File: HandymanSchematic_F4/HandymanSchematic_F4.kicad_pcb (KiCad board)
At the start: 4 copper layers, 55.6 x 45.5 mm, 85 parts, among them J1 SWD Header, J2 PWR, J3 JACKS, J4 FOOTSWITCH, J5 ScopeGroundLoop, Q1 BC847, Q2 2N7002, Q3 2N7002, SW1 RST, SW2 BYP, U1 TL074, U2 TL074, U3 STM32G030F6P6, U4 AMS1117, U5 SSD1306

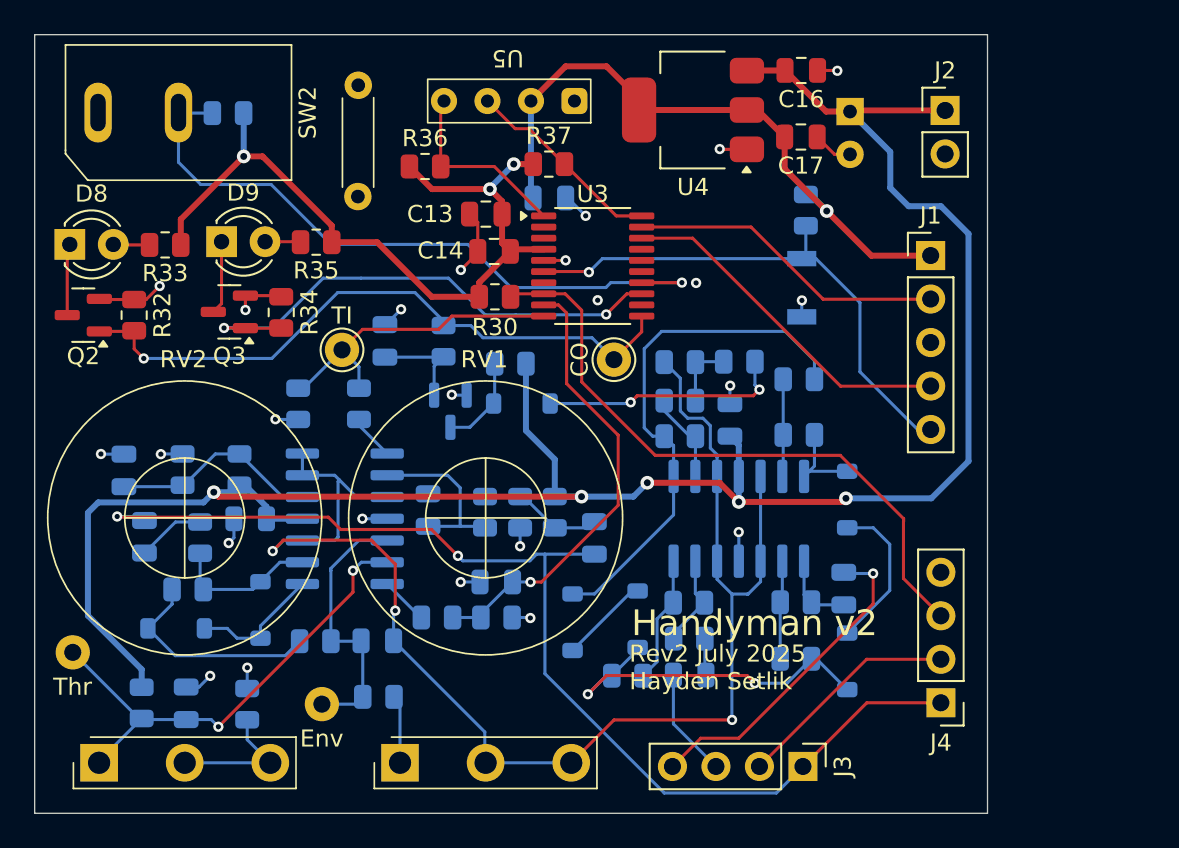
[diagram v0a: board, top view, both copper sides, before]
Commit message: switched to firmware env, new layout
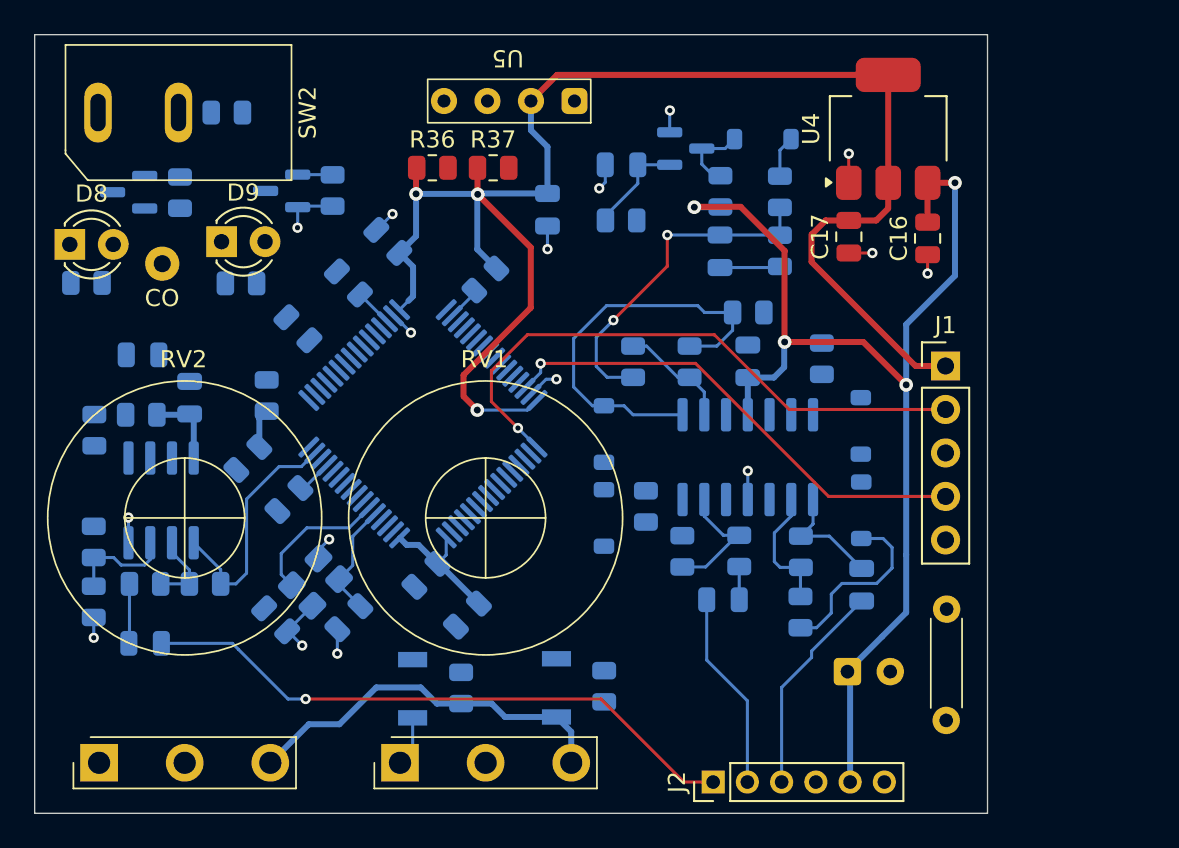
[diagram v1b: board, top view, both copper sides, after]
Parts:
- removed C8: 100n, Capacitor_SMD:C_0805_2012Metric
- removed C9: 22n, Capacitor_SMD:C_0805_2012Metric
- removed D2, D3: 1N4148W, Diode_SMD:D_SOD-123
- removed J3: JACKS, Connector_PinHeader_2.54mm:PinHeader_1x04_P2.54mm_Vertical
- removed J4: FOOTSWITCH, Connector_PinHeader_2.54mm:PinHeader_1x04_P2.54mm_Vertical
- removed R11: 1k, Resistor_SMD:R_0805_2012Metric
- removed R14: 5k6, Resistor_SMD:R_0805_2012Metric
- removed R16, R17: 56k, Resistor_SMD:R_0805_2012Metric
- removed R20: 180k, Resistor_SMD:R_0805_2012Metric
- removed R23, R4, R6: 100k, Resistor_SMD:R_0805_2012Metric
- removed TP1: Thr, TestPoint:TestPoint_THTPad_D2.0mm_Drill1.0mm_VAL
- removed TP3: Env, TestPoint:TestPoint_THTPad_D2.0mm_Drill1.0mm_VAL
- removed TP7: TI, TestPoint:TestPoint_THTPad_D2.0mm_Drill1.0mm_VAL
- removed U1: TL074, Package_SO:SOIC-14_3.9x8.7mm_P1.27mm
- added C15: 4u7, Capacitor_SMD:C_0805_2012Metric, B.Cu at (18.3, 14.5)
- added C18: 10u, Capacitor_SMD:C_0805_2012Metric, B.Cu at (12.4, 24.8)
- added C21: 6p, Capacitor_SMD:C_0805_2012Metric, B.Cu at (14.1, 34.2)
- added C22: 6p, Capacitor_SMD:C_0805_2012Metric, B.Cu at (18.4, 34.0)
- added C23: 1u, Capacitor_SMD:C_0805_2012Metric, B.Cu at (6.45, 35.5)
- added R310: 100k, Resistor_SMD:R_0805_2012Metric, B.Cu at (33.3, 38.1)
- added SW302: BOOT, Button_Switch_SMD:SW_SPST_B3U-1000P, B.Cu at (30.5, 38.1)
- added U6: TL072, Package_SO:SOIC-8_3.9x4.9mm_P1.27mm, B.Cu at (7.38, 27.2)
- added Y1: 16MHz, Crystal:Crystal_SMD_3225-4Pin_3.2x2.5mm, B.Cu at (16.4, 32.0)
- C11: value 1u -> 47n
- C12: value 10n -> 100n
- C13, C14, Q2, Q3, R30, R32, R33, R34, R35, TP8: moved to B.Cu
- C7: value 1u -> 100n
- J2: value PWR -> JACKS; footprint Connector_PinHeader_2.54mm:PinHeader_1x02_P2.54mm_Vertical -> Connector_PinHeader_2.00mm:PinHeader_1x06_P2.00mm_Vertical
- J5: footprint Connector:THT_GND_WIRE -> Connector_Wire:THT_GND_WIRE
- R24: value 470k -> 47k
- R25: value 470k -> 220k
- R26: value 47k -> 330k
- R27: value 180k -> 22
- R28: value 100k -> 47k
- U3: value STM32G030F6P6 -> STM32F411RETx; footprint Package_SO:TSSOP-20_4.4x6.5mm_P0.65mm -> Package_QFP:LQFP-64_10x10mm_P0.5mm; moved to B.Cu
- moved J5 45.8 mm to (53.2, 36.6), turned to 90 degrees
- moved J2 41.5 mm to (39.6, 43.6), turned to 90 degrees
- moved R29 34.4 mm to (24.9, 38.2), turned to 90 degrees
- moved C19 32.7 mm to (47.5, 37.2), turned to 0 degrees
- moved SW1 32.6 mm to (22.1, 38.2)
- moved R24 27.4 mm to (3.45, 33.1), turned to -90 degrees
- moved TP8 27.0 mm to (7.45, 13.4), turned to 180 degrees
- moved C13 23.4 mm to (25.3, 33.9), turned to 45 degrees
- moved C7 23.3 mm to (20.6, 12.1), turned to -45 degrees
- moved R25 22.3 mm to (6.45, 32.1), turned to 0 degrees
- moved D1 20.9 mm to (42.5, 6.10)
- moved Q1 20.6 mm to (38.0, 6.65), turned to 0 degrees
- moved C14 19.3 mm to (22.9, 31.6), turned to 45 degrees
- moved C11 18.3 mm to (40.0, 12.7), turned to -90 degrees
- moved C4 17.2 mm to (34.3, 7.60), turned to 180 degrees
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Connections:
- C11 pad 1: FX_IN -> Net-(C11-Pad1)
- C11 pad 2: Net-(C11-Pad2) -> /Analog/VG
- C12 pad 1: /Analog/VG -> GND
- C12 pad 2: Net-(U1C--) -> +3.3VA
- C5 pad 1: FX_IN -> GND
- C5 pad 2: Net-(C5-Pad2) -> +3.3V
- C7 pad 1: /Analog/Env -> GND
- C7 pad 2: /Analog/VG -> +3.3V
- J2 pad 1: +9V -> FX_IN
- J2 pad 2: GND -> LOOP_IN
- R10 pad 1: Net-(R10-Pad1) -> Net-(C11-Pad1)
- R24 pad 1: Net-(C11-Pad2) -> Net-(U6A-+)
- R24 pad 2: +9V -> GND
- R25 pad 1: GND -> Net-(C23-Pad2)
- R25 pad 2: Net-(C11-Pad2) -> Net-(U6A--)
- R26 pad 1: Net-(C11-Pad2) -> Net-(U6A--)
- R26 pad 2: Net-(U1C--) -> TUNE_IN
- R27 pad 1: Net-(R27-Pad1) -> +3.3V
- R27 pad 2: TUNE_IN -> +3.3VA
- R28 pad 1: GND -> +3.3V
- R28 pad 2: TUNE_IN -> Net-(U6A-+)
- R7 pad 2: Net-(R10-Pad1) -> Net-(C11-Pad1)
- R9 pad 1: Net-(R10-Pad1) -> Net-(C11-Pad1)
- RV1 pad 1: Net-(R14-Pad2) -> GND
- RV1 pad 2: /Analog/VG -> THRESH_IN
- RV1 pad 3: /Analog/VG -> +3.3V
- RV2 pad 1: /Analog/Thresh -> GND
- RV2 pad 2: Net-(R17-Pad1) -> RELEASE_IN
- RV2 pad 3: Net-(R17-Pad1) -> +3.3V
- U3 pad 1: /Digital/SDA -> +3.3V
- U3 pad 10: TUNE_IN -> unconnected-(U3-PC2-Pad10)
- U3 pad 11: CLOSED_OUT -> unconnected-(U3-PC3-Pad11)
- U3 pad 12: unconnected-(U3-PA5-Pad12) -> GND
- U3 pad 13: /Digital/GateLED -> +3.3VA
- U3 pad 14: /Digital/GateByp -> unconnected-(U3-PA0-Pad14)
- U3 pad 15: unconnected-(U3-PB0/PB1/PB2/PA8-Pad15) -> TUNE_IN
- U3 pad 16: unconnected-(U3-PA11/PA9-Pad16) -> THRESH_IN
- U3 pad 17: unconnected-(U3-PA12/PA10-Pad17) -> RELEASE_IN
- U3 pad 18: SWDIO -> GND
- U3 pad 19: SWCLK -> +3.3V
- U3 pad 20: /Digital/SCL -> unconnected-(U3-PA4-Pad20)
- U3 pad 4: +3.3V -> unconnected-(U3-PC15-Pad4)
- U3 pad 5: GND -> Net-(U3-PH0)
- U3 pad 6: NRST -> Net-(U3-PH1)
- U3 pad 7: unconnected-(U3-PA0-Pad7) -> NRST
- U3 pad 8: /Digital/TunerModeIn -> unconnected-(U3-PC0-Pad8)
- U3 pad 9: OPEN_IN -> unconnected-(U3-PC1-Pad9)
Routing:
- net /Analog/VG: track 85.3 -> 3.53 mm, vias 3 -> 0
- net +9V: track 123.0 -> 73.2 mm, vias 5 -> 4
- net +3.3V: track 83.5 -> 125.4 mm, vias 4 -> 3
- net /Digital/GateByp: track 39.8 -> 0.00 mm, vias 1 -> 0
- net CLOSED_OUT: track 37.9 -> 0.00 mm, vias 1 -> 0
- net /Digital/TunerModeIn: track 37.5 -> 2.00 mm
- net NRST: track 31.5 -> 0.00 mm, vias 1 -> 0
- net FX_IN: track 66.0 -> 35.6 mm, vias 2 -> 1
- net /Analog/Thresh: track 28.5 -> 0.00 mm, vias 2 -> 0
- net /Digital/GateLED: track 30.3 -> 2.04 mm, vias 2 -> 0
- net OPEN_IN: track 26.5 -> 0.00 mm, vias 1 -> 0
- net Net-(C11-Pad1): track 0.00 -> 20.0 mm, vias 0 -> 2
- net SWCLK: track 18.6 -> 34.8 mm, vias 0 -> 1
- net /Analog/Env: track 15.9 -> 0.00 mm
- net FX_OUT: track 13.2 -> 0.00 mm
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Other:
- board text removed: "CLK"
- board text removed: "DIO"
- board text removed: "FI"
- board text removed: "FO"
- board text removed: "GND"
- board text removed: "Handyman v2"
- board text removed: "LI"
- board text removed: "LO"
- board text removed: "NRST"
- board text removed: "Rev2 July 2025 Hayden Setlik"
- board text removed: "VCC"

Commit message: prelim routing
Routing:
- net +3.3V: track 125.4 -> 257.9 mm, vias 3 -> 5
- net /Analog/VG: track 3.53 -> 81.8 mm, vias 0 -> 4
- net CLOSED_OUT: track 0.00 -> 77.1 mm, vias 0 -> 1
- net NRST: track 0.00 -> 48.3 mm, vias 0 -> 3
- net +9V: track 73.2 -> 120.4 mm, vias 4 -> 5
- net THRESH_IN: track 0.00 -> 46.8 mm, vias 0 -> 2
- net /Digital/TunerModeIn: track 2.00 -> 44.9 mm, vias 0 -> 1
- net RELEASE_IN: track 0.00 -> 33.5 mm, vias 0 -> 1
- net /Digital/GateByp: track 0.00 -> 32.9 mm, vias 0 -> 2
- net /Digital/SCL: track 0.00 -> 26.7 mm, vias 0 -> 1
- net /Digital/SDA: track 0.00 -> 26.5 mm, vias 0 -> 1
- net /Digital/GateLED: track 2.04 -> 26.6 mm, vias 0 -> 2
- net GND: track 29.6 -> 52.9 mm, vias 16 -> 32
- net /Analog/SumPt: track 10.7 -> 29.5 mm
- net /Digital/BOOT0: track 0.00 -> 13.6 mm
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
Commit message: prettier routing, DRC passing
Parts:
- added TP1: AC, TestPoint:TestPoint_THTPad_D2.0mm_Drill1.0mm_VAL, F.Cu at (31.9, 15.2)
- added TP2: AA, TestPoint:TestPoint_THTPad_D2.0mm_Drill1.0mm_VAL, F.Cu at (47.9, 16.1)
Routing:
- net +9V: track 120.4 -> 129.2 mm
- net /Analog/VG: track 81.8 -> 89.5 mm, vias 4 -> 2
- net +3.3V: track 257.9 -> 264.8 mm
- net /Analog/AmpAnode: track 5.42 -> 10.7 mm
- net GND: track 52.9 -> 50.8 mm, vias 32 -> 39
- net THRESH_IN: track 46.8 -> 45.0 mm
- net /Digital/TunerModeIn: track 44.9 -> 43.2 mm
- net Net-(C11-Pad1): track 20.0 -> 19.0 mm
- net CLOSED_OUT: track 77.1 -> 76.3 mm
- net SWDIO: track 28.7 -> 28.2 mm
- added copper zone on B.Cu, net GND
- added copper zone on F.Cu, net GND

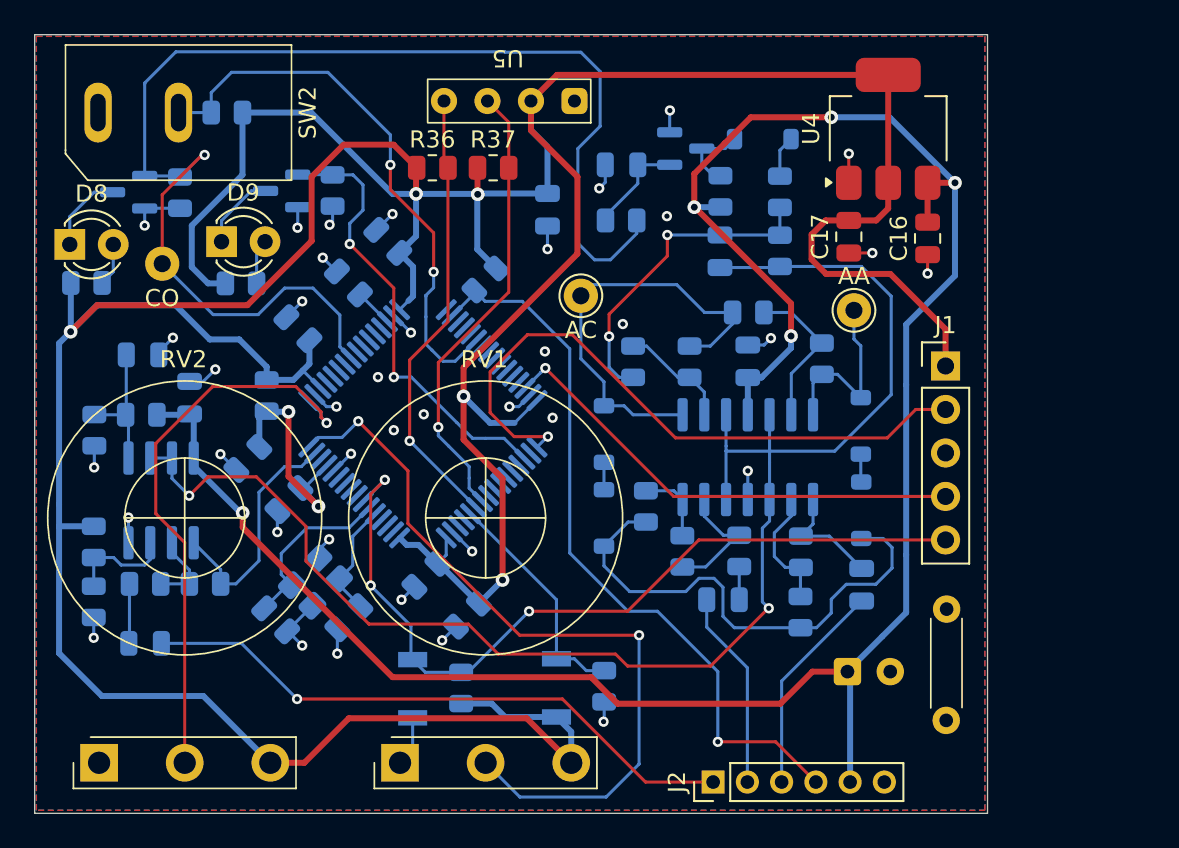
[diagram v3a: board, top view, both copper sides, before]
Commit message: bitstream autocorrelation implemented
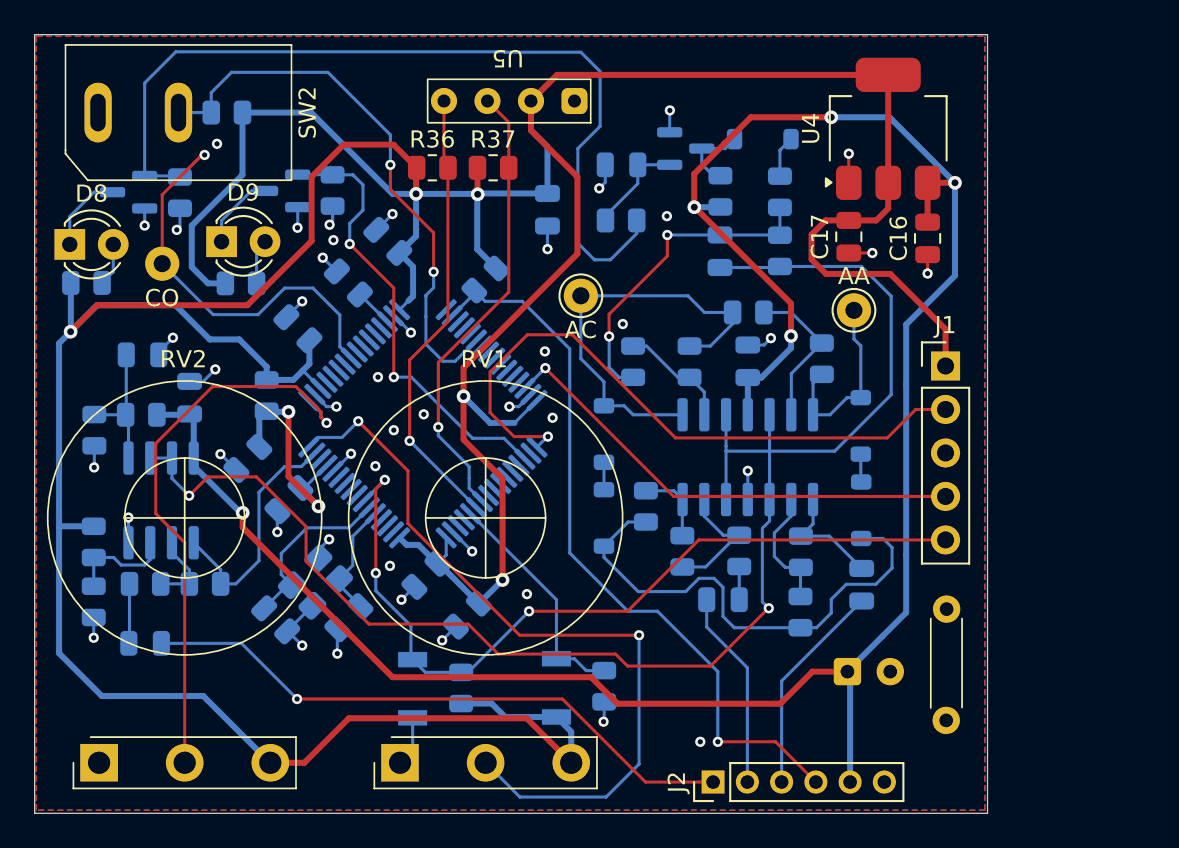
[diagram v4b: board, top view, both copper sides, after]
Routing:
- net GND: track 50.8 -> 50.1 mm, vias 39 -> 46
- net /Analog/AmpCathode: track 25.3 -> 24.8 mm

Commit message: v2 gerbers ready
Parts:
- added TP3: TI, TestPoint:TestPoint_THTPad_D2.0mm_Drill1.0mm_VAL, F.Cu at (16.4, 37.6)
- J2: footprint Connector_PinHeader_2.00mm:PinHeader_1x06_P2.00mm_Vertical -> Connector_PinHeader_2.54mm:PinHeader_1x06_P2.54mm_Vertical
- moved J5 30.6 mm to (53.5, 6.05)
- moved C19 4.83 mm to (52.3, 37.4), turned to 90 degrees
- moved U4 1.58 mm to (48.3, 5.67)
- moved C16 1.50 mm to (50.6, 11.8)
- moved J2 1.12 mm to (38.5, 43.3)
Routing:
- net TUNE_IN: track 14.1 -> 24.0 mm
- net +3.3V: track 264.8 -> 255.6 mm, vias 5 -> 6
- net +9V: track 129.2 -> 137.1 mm
- net /Digital/GateByp: track 32.9 -> 35.0 mm
- net FX_IN: track 35.6 -> 36.4 mm
- net LOOP_IN: track 11.3 -> 12.0 mm
- net /Analog/SumPt: track 29.0 -> 29.7 mm
- net GND: vias 46 -> 74
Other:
- board text added: "+9V"
- board text added: "GND"
- board text added: "Handyman V2"
- board text added: "L_IN"
- board text added: "L_OUT"
- board text added: "MODE"
- board text added: "Rev 1- 02/2026 Hayden Setlik"
- board text added: "TUNE"

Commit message: minor tweaks for DRC
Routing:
- net GND: track 50.1 -> 53.8 mm, vias 74 -> 76
- net SWDIO: track 28.2 -> 30.5 mm
- net +3.3V: track 255.6 -> 257.6 mm
- net CLOSED_OUT: track 76.0 -> 76.5 mm
